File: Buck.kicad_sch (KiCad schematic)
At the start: 15 parts, among them J1 IN, J2 OUT, J3 Measure, U1 LT1936

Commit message: small tweaks trace layout
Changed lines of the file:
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@@
 	(paper "A4")
 	(junction
+		(at 137.16 87.63)
+		(diameter 0)
+		(color 0 0 0 0)
+	)
+	(junction
 		(at 62.23 87.63)
 		(diameter 0)
@@
 	(wire
 		(pts
+			(xy 137.16 87.63) (xy 139.7 87.63)
+		)
+		(stroke
+			(width 0)
+			(type default)
+		)
+	)
+	(wire
+		(pts
 			(xy 83.82 104.14) (xy 83.82 110.49)
 		)
@@
 	(wire
 		(pts
-			(xy 128.27 87.63) (xy 139.7 87.63)
+			(xy 128.27 87.63) (xy 137.16 87.63)
 		)
 		(stroke
@@
 		(pts
 			(xy 101.6 93.98) (xy 101.6 96.9578)
+		)
+		(stroke
+			(width 0)
+			(type default)
+		)
+	)
+	(wire
+		(pts
+			(xy 137.16 86.36) (xy 137.16 87.63)
 		)
 		(stroke
@@
 	(global_label "Uout"
 		(shape input)
-		(at 137.16 87.63 90)
+		(at 137.16 86.36 90)
 		(fields_autoplaced yes)
 		(effects
@@
 		)
 		(property "Intersheetrefs" "${INTERSHEET_REFS}"
-			(at 137.16 80.2906 90)
+			(at 137.16 79.0206 90)
 			(effects
 				(font

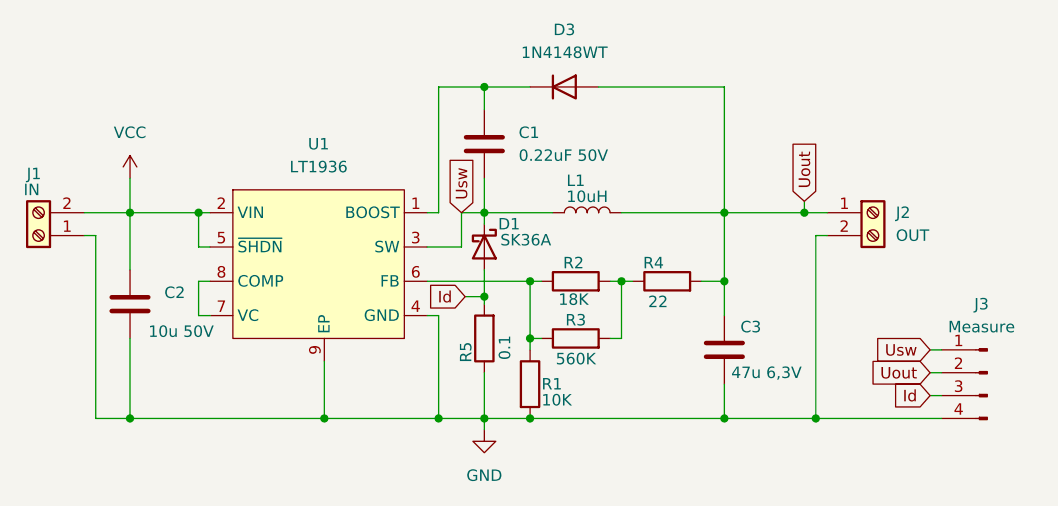
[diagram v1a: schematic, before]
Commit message: addes extra silkscreen for info
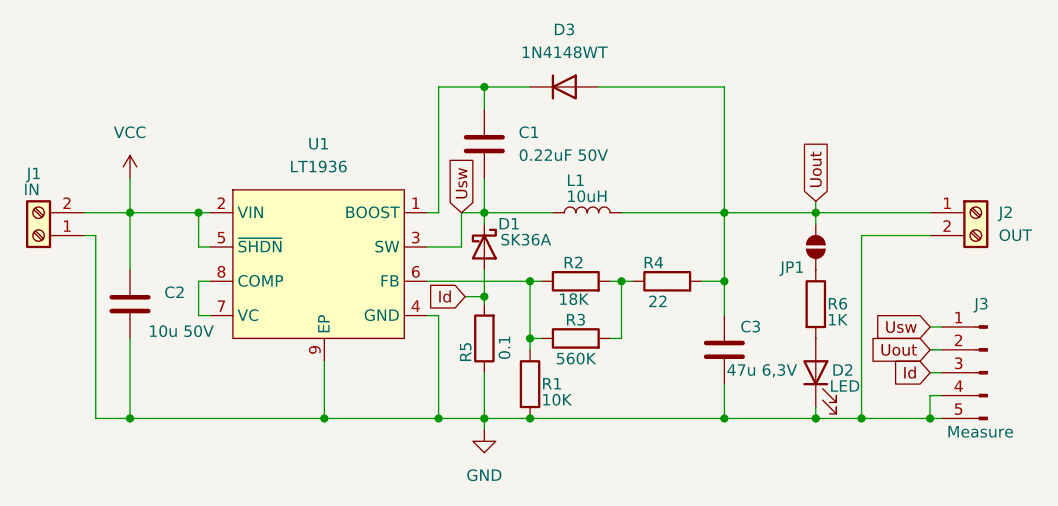
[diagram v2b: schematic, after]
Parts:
- added D2: LED, LED_SMD:LED_0805_2012Metric_Pad1.15x1.40mm_HandSolder, symbol Device:LED
- added JP1: SolderJumper_2_Open, Jumper:SolderJumper-2_P1.3mm_Open_TrianglePad1.0x1.5mm, symbol Jumper:SolderJumper_2_Open
- added R6: 1K, Resistor_SMD:R_1206_3216Metric_Pad1.30x1.75mm_HandSolder, symbol Device:R
- J3: footprint Connector_PinHeader_2.54mm:PinHeader_1x04_P2.54mm_Vertical -> Connector_PinHeader_2.54mm:PinHeader_1x05_P2.54mm_Vertical; symbol Connector:Conn_01x04_Pin -> Connector:Conn_01x05_Pin
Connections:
- net GND: now also J3.5 (Pin_5), D2.1 (K)
- net Uout: now also JP1.1 (A)
- new net: JP1.2 (B), R6.1
- new net: D2.2 (A), R6.2
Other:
- moved on the sheet: J2
